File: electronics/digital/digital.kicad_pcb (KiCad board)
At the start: 2 copper layers, 59 parts, among them J1 USB_A, J2 USB_A, J3 RJ45, P1 POWER_IN, P10 AMP_POWER_OUT, P11 CONTROL, P2 3V3_IN, P3 USB_CABLE, P4 USB_CABLE, P5 NETWORK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

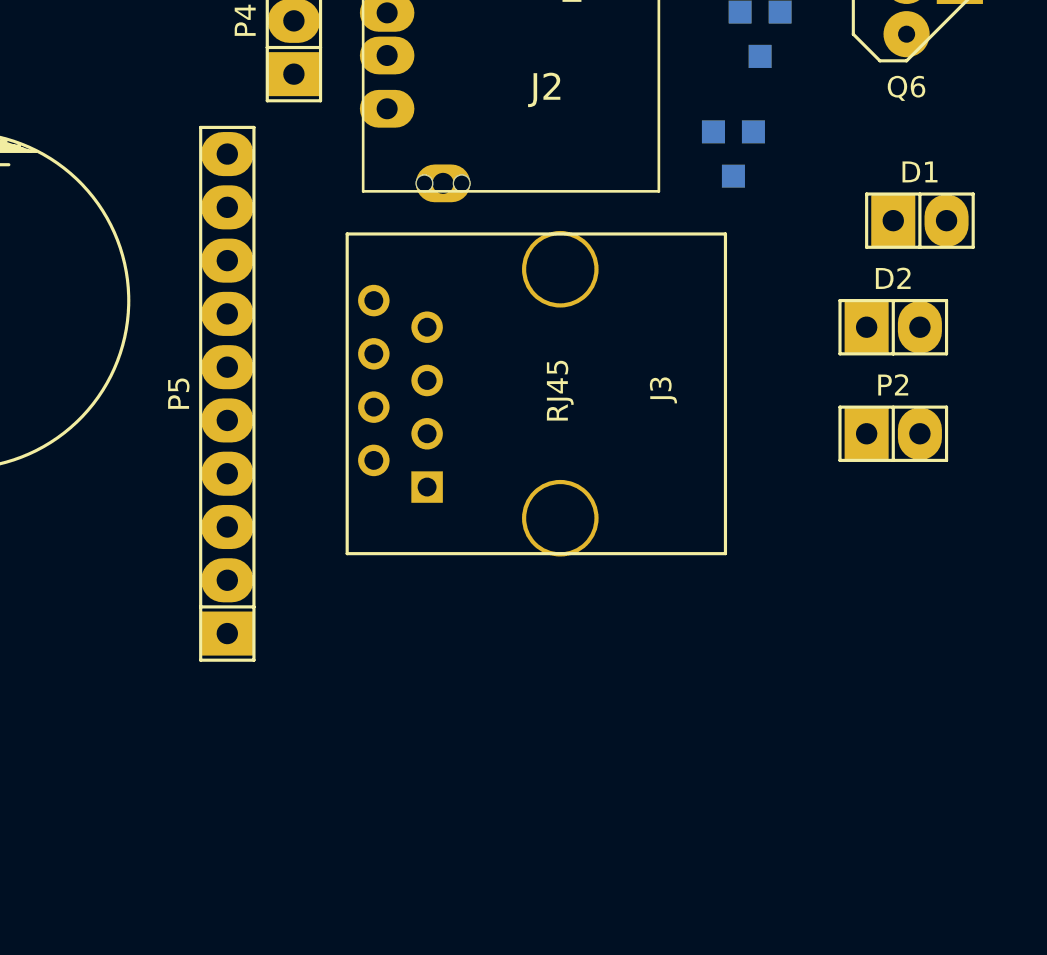
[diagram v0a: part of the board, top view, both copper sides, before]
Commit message: add rj45
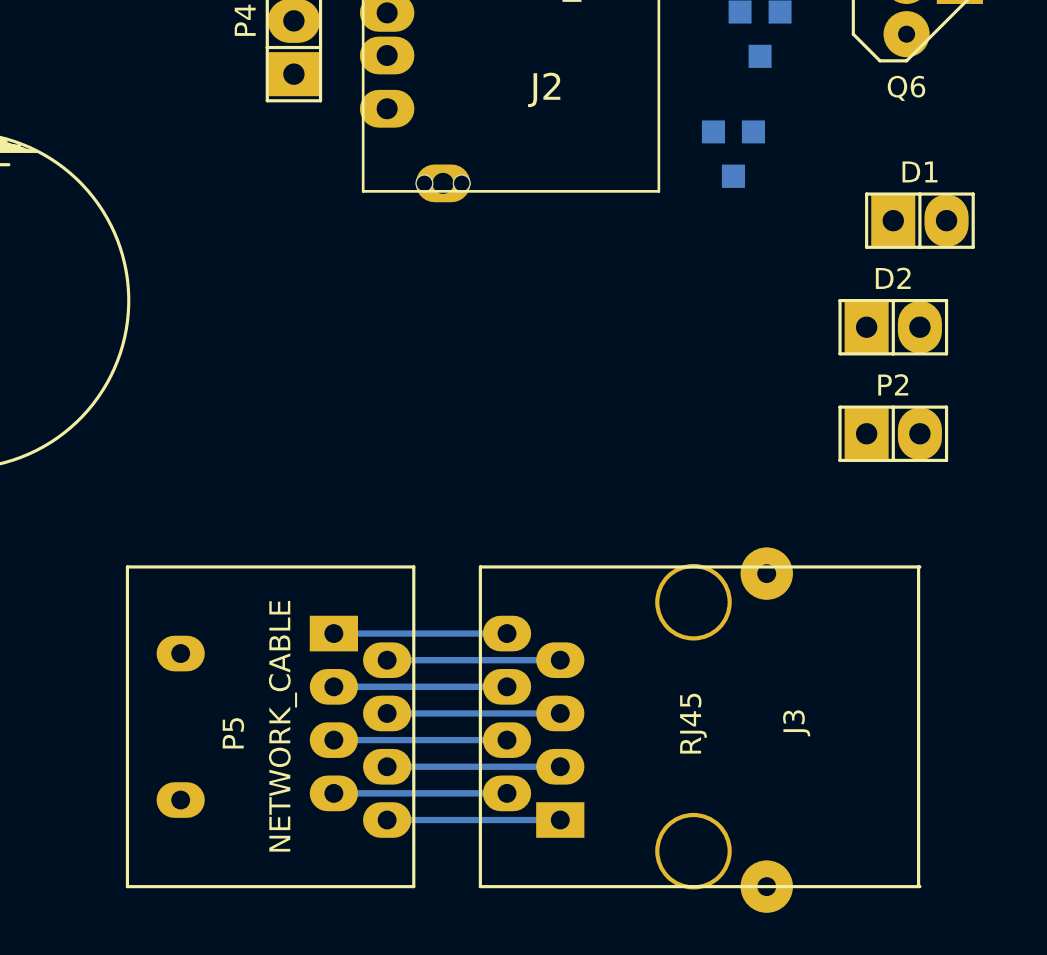
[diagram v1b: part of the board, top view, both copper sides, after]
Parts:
- J3: footprint Connect:RJ45_8 -> rj45:RJ45_8_BIG
- P5: value NETWORK -> NETWORK_CABLE; footprint Pin_Headers:Pin_Header_Straight_1x10 -> rj45:RJ45_SOLDER
- moved J3 17.1 mm to (191.8, 149.2)
- moved P5 15.9 mm to (168.3, 149.2), turned to 270 degrees
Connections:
- P5 pad 1: GND -> Net-(J3-Pad8)
- P5 pad 2: Net-(J3-Pad1) -> Net-(J3-Pad7)
- P5 pad 3: Net-(J3-Pad2) -> Net-(J3-Pad6)
- P5 pad 4: Net-(J3-Pad3) -> Net-(J3-Pad5)
- P5 pad 6: Net-(J3-Pad5) -> Net-(J3-Pad3)
- P5 pad 7: Net-(J3-Pad6) -> Net-(J3-Pad2)
- P5 pad 8: Net-(J3-Pad7) -> Net-(J3-Pad1)
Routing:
- net Net-(J3-Pad8): track 0.00 -> 8.25 mm
- net Net-(J3-Pad7): track 0.00 -> 8.25 mm
- net Net-(J3-Pad6): track 0.00 -> 8.25 mm
- net Net-(J3-Pad5): track 0.00 -> 8.25 mm
- net Net-(J3-Pad4): track 0.00 -> 8.25 mm
- net Net-(J3-Pad3): track 0.00 -> 8.25 mm
- net Net-(J3-Pad2): track 0.00 -> 8.25 mm
- net Net-(J3-Pad1): track 0.00 -> 8.25 mm
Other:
- net class Default: clearance 0.254 -> 0; trace_width 0.254 -> 0.3
- rule trace_clearance: 0.254 -> 0

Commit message: add fuse
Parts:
- added F1: FUSE, Capacitors_ThroughHole:Capacitor6MMDiscRM5, F.Cu at (245.1, 59.1)
- moved P1 143.0 mm to (255.3, 59.1), turned to 180 degrees
- moved P7 128.7 mm to (233.7, 79.4), turned to 270 degrees
- moved C1 103.0 mm to (233.7, 60.3)
- moved P6 102.3 mm to (249.6, 79.4), turned to 270 degrees
- moved P8 95.9 mm to (243.2, 79.4), turned to 270 degrees
- moved J1 72.4 mm to (249.6, 97.2)
- moved J2 72.4 mm to (249.6, 115.6)
- moved P3 72.4 mm to (245.1, 95.9)
- moved P4 72.4 mm to (245.1, 114.9)
- moved J3 63.4 mm to (254.0, 137.2)
- moved P5 63.4 mm to (230.5, 137.2)
- moved C2 57.2 mm to (79.4, 92.7)
- moved C5 57.2 mm to (77.5, 99.1)
- moved C8 57.2 mm to (77.5, 104.8)
- moved D1 57.2 mm to (145.4, 121.9)
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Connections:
- P1 pad 1: +5V -> Net-(F1-Pad1)
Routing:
- net +5V: track 0.00 -> 13.2 mm
- net Net-(F1-Pad1): track 0.00 -> 5.73 mm
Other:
- net class Default: via_dia 0.889 -> 2.2

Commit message: route led drivers
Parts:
- moved R1 74.2 mm to (199.4, 144.1), turned to 180 degrees
- moved R15 74.1 mm to (161.3, 164.5)
- moved Q1 70.9 mm to (199.4, 141.6)
- moved R13 69.3 mm to (214.0, 136.5)
- moved D2 66.7 mm to (208.9, 142.9), turned to 90 degrees
- moved D1 63.8 mm to (208.9, 127.6), turned to 90 degrees
- moved Q2 63.0 mm to (199.4, 126.4)
- moved R16 62.4 mm to (157.5, 153.0)
- moved R18 56.6 mm to (160.7, 158.8)
- moved R2 56.4 mm to (199.4, 128.9), turned to 180 degrees
- moved R5 55.2 mm to (199.4, 136.5)
- moved R17 55.0 mm to (157.5, 149.2)
- moved Q3 54.1 mm to (188.0, 134.0), turned to 180 degrees
- moved R12 53.3 mm to (214.0, 121.3)
- moved R4 48.1 mm to (199.4, 125.1)
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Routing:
- net Net-(P6-Pad6): track 0.00 -> 45.1 mm
- net Net-(P6-Pad4): track 0.00 -> 29.0 mm
- net Net-(P6-Pad8): track 0.00 -> 28.4 mm
- net Net-(Q3-Pad2): track 0.00 -> 17.6 mm
- net Net-(Q4-Pad2): track 0.00 -> 17.6 mm
- net Net-(Q1-Pad1): track 0.00 -> 16.2 mm
- net Net-(Q2-Pad1): track 0.00 -> 16.2 mm
- net Net-(P6-Pad2): track 0.00 -> 13.2 mm
- net Net-(P6-Pad10): track 0.00 -> 12.0 mm
- net GND: track 0.00 -> 10.2 mm
- net /LED_VCC: track 0.00 -> 8.43 mm
- net Net-(Q2-Pad3): track 0.00 -> 6.19 mm
- net Net-(Q1-Pad3): track 0.00 -> 6.19 mm
- net Net-(D2-Pad1): track 0.00 -> 4.44 mm
- net Net-(P6-Pad9): track 0.00 -> 3.81 mm
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
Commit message: arrange transistors
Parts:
- removed R12, R13: 10, Resistors_ThroughHole:Resistor_Horizontal_RM10mm
- Q8: footprint Transistors_TO-220:TO-220_FET-GDS_Vertical -> SMD_Packages:DPAK-2-1EP_GDS; moved to B.Cu
- moved P11 191.1 mm to (236.2, 159.4)
- moved R14 78.2 mm to (189.9, 150.5)
- moved Q10 75.9 mm to (192.4, 108.0), turned to 270 degrees
- moved P10 75.6 mm to (189.9, 158.1)
- moved Q8 73.6 mm to (215.9, 118.1)
- moved R18 62.9 mm to (204.5, 113.7)
- moved R11 62.5 mm to (189.9, 154.3), turned to 180 degrees
- moved R16 58.9 mm to (204.5, 117.5), turned to 180 degrees
- moved R19 47.1 mm to (204.5, 101.6), turned to 180 degrees
- moved R15 46.7 mm to (204.5, 146.7)
- moved Q7 41.5 mm to (200.7, 108.0), turned to 270 degrees
- moved Q5 33.0 mm to (189.9, 151.8)
- moved R17 32.5 mm to (189.9, 146.7)
- moved Q6 32.4 mm to (178.4, 149.9), turned to 270 degrees
- moved D1 18.0 mm to (191.1, 130.2), turned to 0 degrees
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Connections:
- Q1 pad 3: Net-(Q1-Pad3) -> Net-(D2-Pad1)
- Q2 pad 3: Net-(Q2-Pad3) -> Net-(D1-Pad1)
- R1 pad 1: Net-(D2-Pad1) -> Net-(D2-Pad2)
- R1 pad 2: Net-(Q1-Pad3) -> Net-(Q8-PadD)
- R2 pad 1: Net-(D1-Pad1) -> Net-(Q8-PadD)
- R2 pad 2: Net-(Q2-Pad3) -> Net-(D1-Pad2)
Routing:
- net /LED_VCC: track 8.43 -> 52.8 mm
- net GND: track 10.2 -> 47.8 mm
- net Net-(Q6-Pad2): track 0.00 -> 20.5 mm
- net Net-(Q8-PadD): track 0.00 -> 18.8 mm
- net Net-(Q10-Pad1): track 0.00 -> 15.1 mm
- net Net-(Q10-Pad2): track 0.00 -> 14.8 mm
- net Net-(Q5-Pad1): track 0.00 -> 9.56 mm
- net Net-(D2-Pad2): track 0.00 -> 6.98 mm
- net Net-(D1-Pad2): track 0.00 -> 6.98 mm
- net Net-(P10-Pad1): track 0.00 -> 6.88 mm
- net Net-(Q2-Pad1): track 16.2 -> 9.56 mm
- net Net-(Q1-Pad1): track 16.2 -> 9.56 mm
- net Net-(Q5-Pad3): track 0.00 -> 6.19 mm
- net Net-(Q2-Pad3): track 6.19 -> 0.00 mm
- net Net-(Q1-Pad3): track 6.19 -> 0.00 mm
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
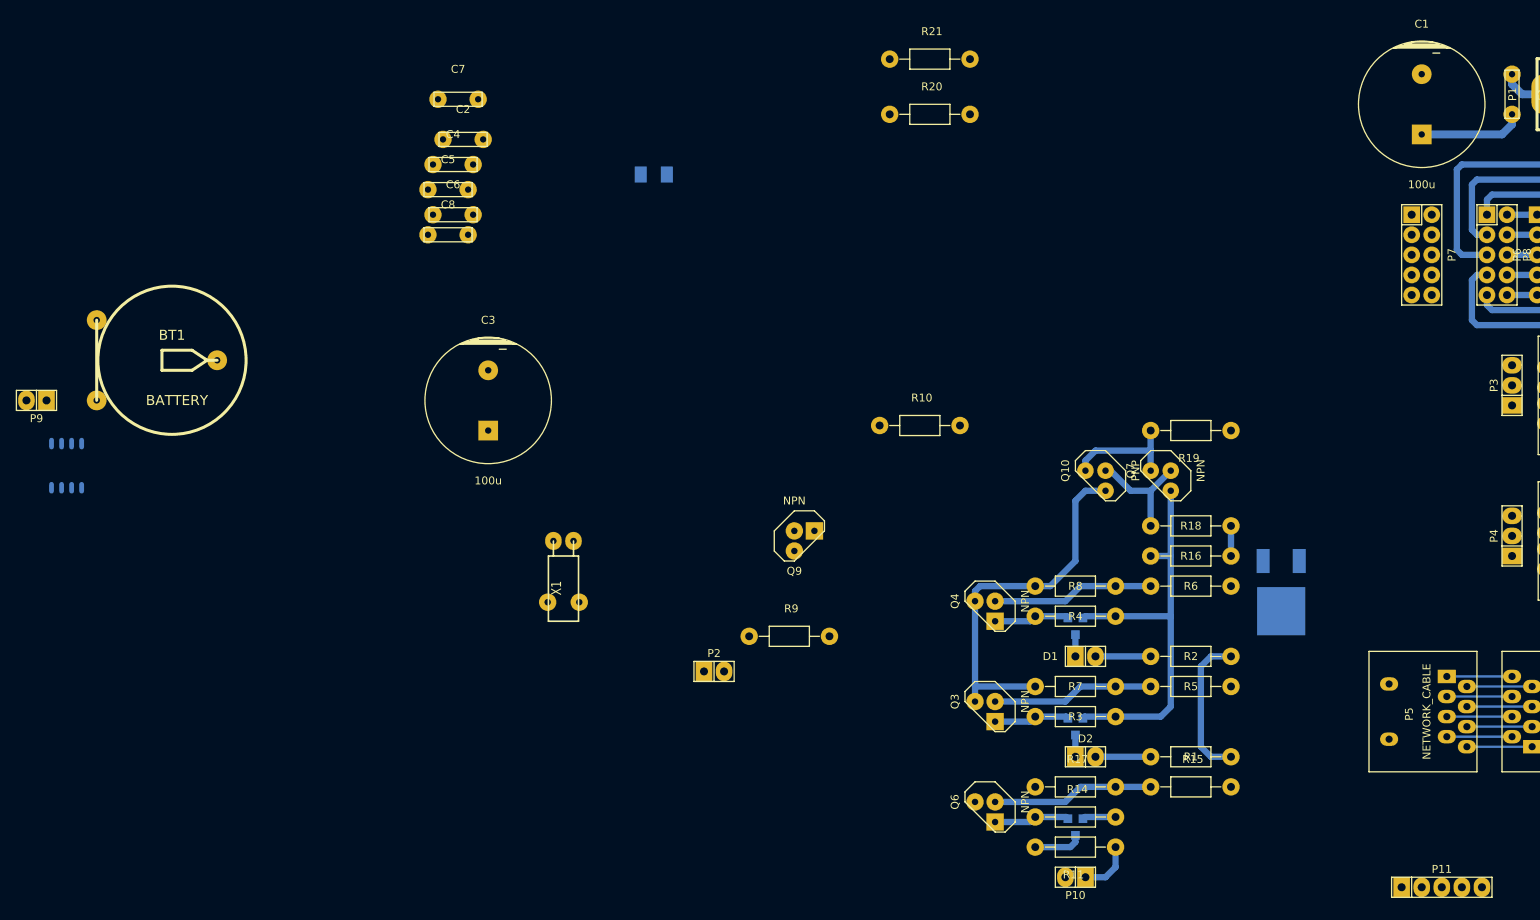
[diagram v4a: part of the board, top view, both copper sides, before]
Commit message: drivers are all routed
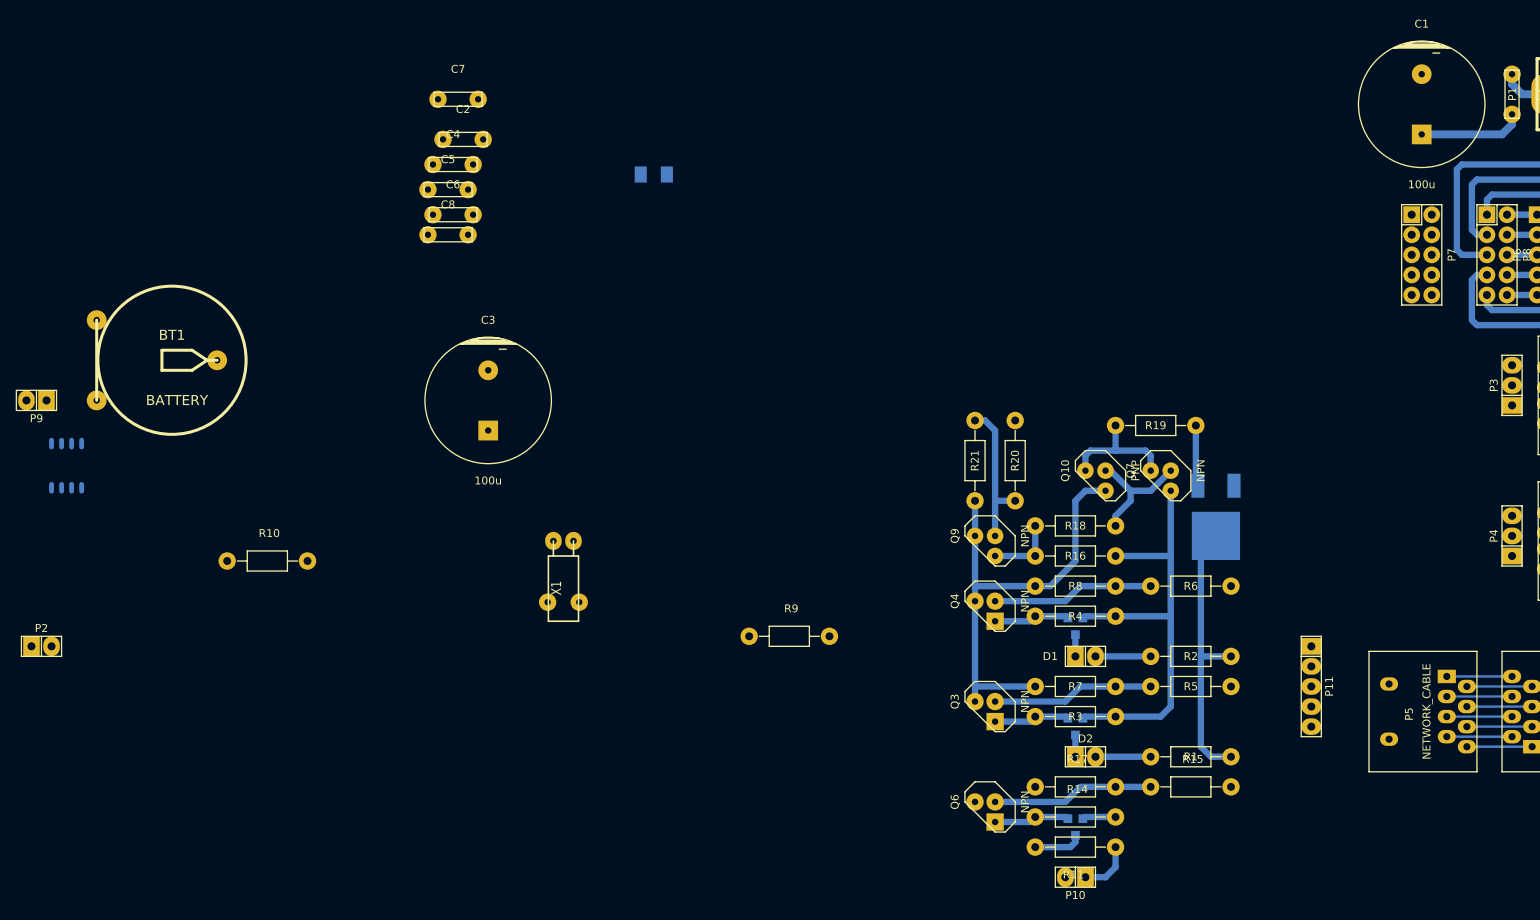
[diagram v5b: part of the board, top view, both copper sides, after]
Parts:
- moved P2 85.1 mm to (59.1, 128.9)
- moved R10 84.3 mm to (87.6, 118.1)
- moved R21 51.1 mm to (177.2, 105.4), turned to 90 degrees
- moved R20 45.1 mm to (182.2, 105.4), turned to 90 degrees
- moved P11 30.3 mm to (219.7, 134.0), turned to 270 degrees
- moved Q9 22.9 mm to (178.4, 116.2), turned to 270 degrees
- moved R16 14.6 mm to (189.9, 117.5), turned to 0 degrees
- moved R18 14.6 mm to (189.9, 113.7), turned to 180 degrees
- moved Q8 12.6 mm to (207.6, 108.6)
- moved R19 4.49 mm to (200.0, 101.0)
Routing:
- net Net-(Q9-Pad2): track 0.00 -> 18.9 mm
- net Net-(Q8-PadD): track 18.8 -> 35.6 mm
- net GND: track 47.8 -> 59.0 mm
- net Net-(Q8-PadG): track 0.00 -> 7.73 mm
- net Net-(Q9-Pad3): track 3.81 -> 8.89 mm
- net /LED_VCC: track 52.8 -> 57.2 mm
- net Net-(Q10-Pad2): track 14.8 -> 15.6 mm
- net Net-(Q10-Pad1): track 15.1 -> 15.8 mm

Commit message: sort of shaped up
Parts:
- C2, C4: footprint Capacitors_ThroughHole:Capacitor6MMDiscRM5 -> SMD_Packages:SMD-1206; moved to B.Cu
- moved P2 176.9 mm to (234.3, 104.8)
- moved P9 159.2 mm to (212.7, 137.2), turned to 0 degrees
- moved U1 151.8 mm to (212.1, 130.2), turned to 0 degrees
- moved BT1 144.6 mm to (216.5, 125.1)
- moved C7 137.0 mm to (246.4, 85.1), turned to 270 degrees
- moved C6 136.7 mm to (245.1, 101.6)
- moved C4 124.3 mm to (234.3, 84.5), turned to 180 degrees
- moved C2 121.9 mm to (234.3, 66.7), turned to 180 degrees
- moved C3 119.5 mm to (234.3, 84.5), turned to 90 degrees
- moved P10 105.5 mm to (210.2, 54.6), turned to 0 degrees
- moved C8 104.5 mm to (203.2, 125.1), turned to 90 degrees
- moved R10 102.9 mm to (177.2, 67.3)
- moved L1 101.8 mm to (238.1, 74.9), turned to 270 degrees
- moved R11 98.0 mm to (210.2, 58.4), turned to 0 degrees
- moved Q6 97.1 mm to (221.6, 62.9), turned to 90 degrees
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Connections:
- X1 pad 1: Net-(C8-Pad1) -> Net-(C8-Pad2)
- X1 pad 2: Net-(C8-Pad2) -> Net-(C8-Pad1)
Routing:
- net GND: track 59.0 -> 120.7 mm
- net Net-(BT1-Pad1): track 0.00 -> 20.8 mm
- net Net-(C8-Pad2): track 0.00 -> 16.0 mm
- net Net-(C8-Pad1): track 0.00 -> 10.8 mm
- net /LED_VCC: track 57.2 -> 67.3 mm
- net +5V: track 17.4 -> 23.1 mm
- net /SCL: track 0.00 -> 4.72 mm
- net /SDA: track 0.00 -> 4.19 mm
- net Net-(F1-Pad1): track 5.73 -> 6.89 mm

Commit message: work on pcb
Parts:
- moved R9 73.8 mm to (211.5, 143.5)
- moved R10 71.2 mm to (196.2, 135.9)
- moved P11 41.8 mm to (189.9, 114.3), turned to 90 degrees
- moved C5 38.2 mm to (179.7, 114.3)
- moved P2 17.3 mm to (229.2, 121.3), turned to 270 degrees
- moved C7 8.98 mm to (247.7, 76.2), turned to 90 degrees
- moved C6 7.43 mm to (247.7, 94.6), turned to 90 degrees
- moved P3 3.24 mm to (243.8, 76.2)
- moved P4 3.17 mm to (243.8, 94.6)
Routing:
- net +5V: track 23.1 -> 81.7 mm
- net Net-(J2-Pad2): track 0.00 -> 8.83 mm
- net Net-(J1-Pad2): track 0.00 -> 8.83 mm
- net Net-(J2-Pad3): track 0.00 -> 8.53 mm
- net Net-(J1-Pad3): track 0.00 -> 7.99 mm
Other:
- net class Default: trace_width 0.3 -> 0.8
- net class power added: clearance 0, trace_width 1, via_dia 2.2, via_drill 0.635

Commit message: placed everything
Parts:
- P11: footprint Pin_Headers:Pin_Header_Straight_1x05 -> Pin_Headers:Pin_Header_Straight_1x04
- moved P10 62.6 mm to (203.2, 116.8), turned to 180 degrees
- moved C5 59.8 mm to (238.1, 101.6), turned to 180 degrees
- moved R11 55.1 mm to (203.2, 113.0), turned to 180 degrees
- moved Q6 54.6 mm to (191.8, 108.6), turned to 270 degrees
- moved R21 54.0 mm to (190.5, 64.1), turned to 90 degrees
- moved R10 51.2 mm to (236.9, 104.8), turned to 180 degrees
- moved R19 50.2 mm to (198.1, 61.6), turned to 270 degrees
- moved Q5 50.0 mm to (203.2, 110.5), turned to 0 degrees
- moved R20 48.4 mm to (221.0, 59.1), turned to 0 degrees
- moved R14 47.5 mm to (203.2, 109.2), turned to 0 degrees
- moved Q8 46.6 mm to (221.0, 67.3), turned to 0 degrees
- moved R15 45.2 mm to (217.8, 105.4), turned to 0 degrees
- moved R9 43.7 mm to (236.9, 108.0), turned to 180 degrees
- moved P11 41.0 mm to (228.0, 99.1)
- moved Q7 40.8 mm to (214.0, 66.7), turned to 270 degrees
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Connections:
- P11 pad 1: GND -> /LED_PWM
- P11 pad 2: /LED_PWM -> /LED_SEL_1
- P11 pad 3: /AMP_SEL -> /LED_SEL_2
- P11 pad 4: /LED_SEL_1 -> /AMP_SEL
- P7 pad 1: +5V -> +3.3VP
- P7 pad 3: +5V -> +3.3VP
- P7 pad 7: +3.3VP -> +5V
- P7 pad 9: +3.3VP -> +5V
- U1 pad 1: Net-(C8-Pad1) -> Net-(C8-Pad2)
- U1 pad 2: Net-(C8-Pad2) -> Net-(C8-Pad1)
- U1 pad 7: (no net) -> Net-(U1-Pad7)
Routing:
- net +5V: track 81.7 -> 134.5 mm
- net GND: track 120.7 -> 165.6 mm
- net /AMP_SEL: track 0.00 -> 38.5 mm
- net +3.3VP: track 0.00 -> 35.6 mm
- net /LED_SEL_1: track 0.00 -> 26.9 mm
- net Net-(Q8-PadG): track 7.73 -> 30.8 mm
- net Net-(Q9-Pad2): track 18.9 -> 40.6 mm
- net /SDA: track 4.19 -> 16.9 mm
- net Net-(C8-Pad1): track 10.8 -> 21.2 mm
- net /SCL: track 4.72 -> 13.6 mm
- net Net-(C8-Pad2): track 16.0 -> 9.93 mm
- net /LED_SEL_2: track 0.00 -> 5.72 mm
- net Net-(Q10-Pad1): track 15.8 -> 20.7 mm
- net /LED_PWM: track 0.00 -> 4.60 mm
- net Net-(BT1-Pad1): track 20.8 -> 24.5 mm
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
